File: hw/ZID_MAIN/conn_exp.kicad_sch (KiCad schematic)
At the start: 31 parts, among them J10 USB-C PWR ONLY, J8 BRK EXP SOCKET, J9 Z80-TARGET, U24 74AHCT125

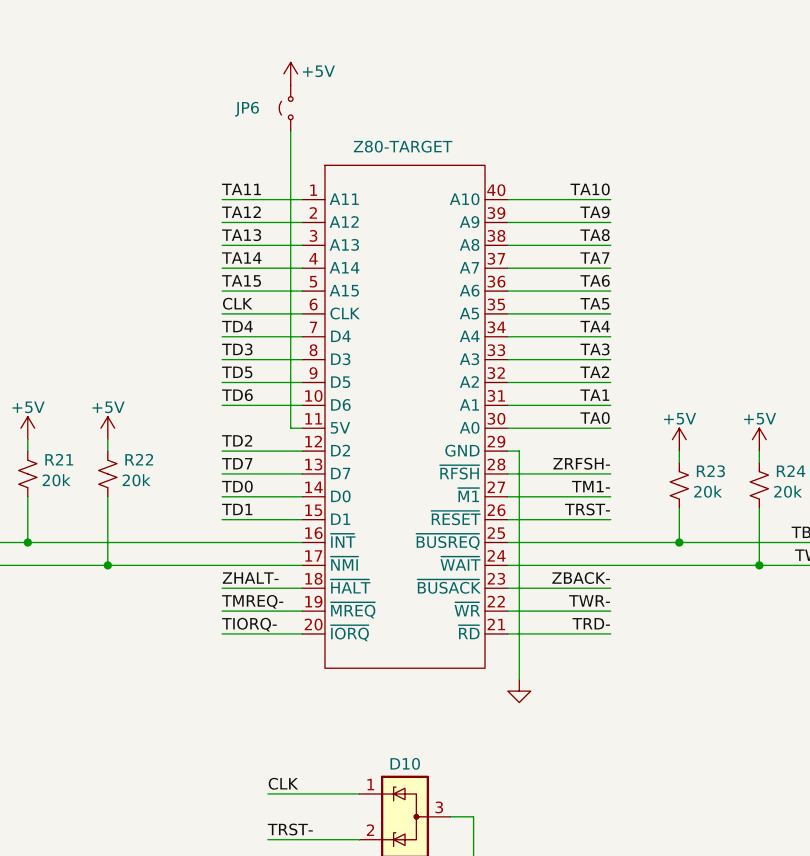
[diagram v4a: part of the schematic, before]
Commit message: Footprints assigned
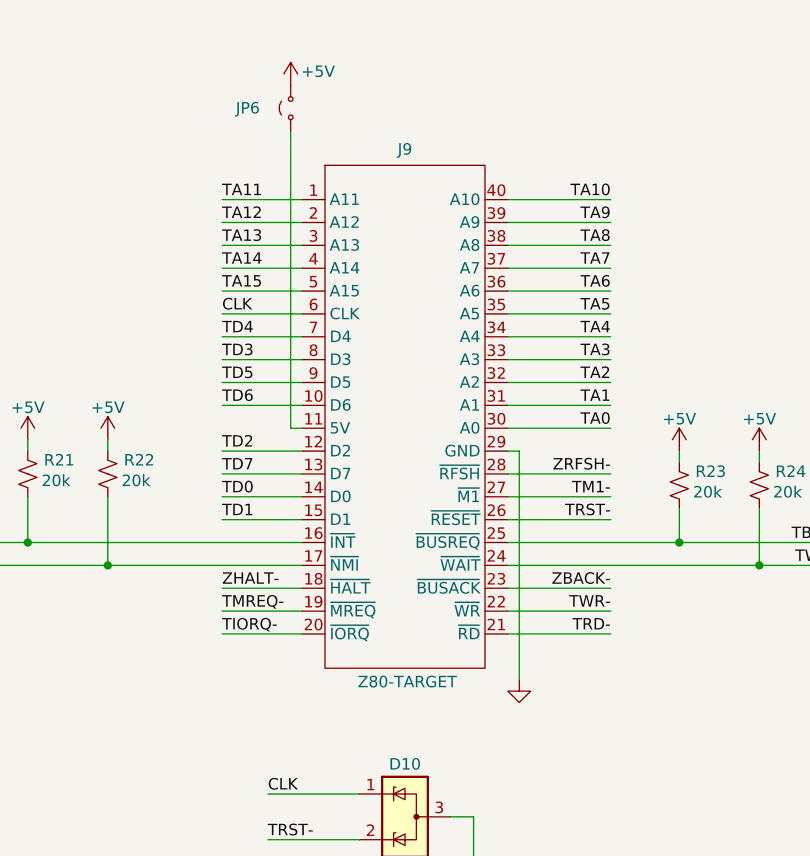
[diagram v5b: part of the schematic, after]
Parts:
- D1: value LED RED -> LED BLUE
- D10, D11: footprint Package_TO_SOT_SMD:SOT-23-3 -> Package_TO_SOT_SMD:SOT-323_SC-70
- D12: footprint Diode_SMD:D_SOD-523 -> AES_Library:DO-214AB-AES
- D2: value LED RED -> LED YELLOW
- D4: value LED RED -> LED ORANGE
- H1, H2, H3, H4: footprint (none) -> MountingHole:MountingHole_3.2mm_M3
- J8: footprint (none) -> Connector_PinSocket_2.54mm:PinSocket_1x28_P2.54mm_Vertical
- J9: footprint Connector_PinHeader_2.00mm:PinHeader_2x20_P2.00mm_Vertical -> AES_Library:CviLux_CF25401D0-05-NH_FFC-FPC-AES
- JP5, JP6, JP7: footprint (none) -> Connector_PinHeader_2.00mm:PinHeader_1x02_P2.00mm_Vertical
- R19, R20, R21, R22, R23, R24, R25, R26: footprint (none) -> Resistor_SMD:R_0805_2012Metric
- U24: footprint (none) -> Package_SO:SOIC-14_3.9x8.7mm_P1.27mm
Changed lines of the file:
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@@
 			)
 		)
-		(property "Footprint" ""
+		(property "Footprint" "MountingHole:MountingHole_3.2mm_M3"
 			(at 391.16 275.59 0)
 			(effects
@@
 			)
 		)
-		(property "Footprint" "Diode_SMD:D_SOD-523"
+		(property "Footprint" "AES_Library:DO-214AB-AES"
 			(at 256.54 268.605 0)
 			(effects
@@
 			)
 		)
-		(property "Footprint" ""
+		(property "Footprint" "Resistor_SMD:R_0805_2012Metric"
 			(at 187.96 62.23 0)
 			(effects
@@
 			)
 		)
-		(property "Value" "LED RED"
+		(property "Value" "LED ORANGE"
 			(at 217.424 76.454 0)
 			(effects
@@
 			)
 		)
-		(property "Footprint" ""
+		(property "Footprint" "MountingHole:MountingHole_3.2mm_M3"
 			(at 398.78 275.59 0)
 			(effects
@@
 			)
 		)
-		(property "Footprint" ""
+		(property "Footprint" "Connector_PinHeader_2.00mm:PinHeader_1x02_P2.00mm_Vertical"
 			(at 107.95 27.94 0)
 			(effects
@@
 			)
 		)
-		(property "Footprint" ""
+		(property "Footprint" "Connector_PinHeader_2.00mm:PinHeader_1x02_P2.00mm_Vertical"
 			(at 290.83 274.32 0)
 			(effects
@@
 			)
 		)
-		(property "Footprint" ""
+		(property "Footprint" "MountingHole:MountingHole_3.2mm_M3"
 			(at 383.54 275.59 0)
 			(effects
@@
 			)
 		)
-		(property "Footprint" "Package_TO_SOT_SMD:SOT-23-3"
+		(property "Footprint" "Package_TO_SOT_SMD:SOT-323_SC-70"
 			(at 130.81 91.44 0)
 			(effects
@@
 			)
 		)
-		(property "Footprint" ""
+		(property "Footprint" "Package_SO:SOIC-14_3.9x8.7mm_P1.27mm"
 			(at 199.39 64.77 0)
 			(effects
@@
 			)
 		)
-		(property "Footprint" ""
+		(property "Footprint" "Resistor_SMD:R_0805_2012Metric"
 			(at 187.96 48.26 0)
 			(effects
@@
 			)
 		)
-		(property "Footprint" ""
+		(property "Footprint" "Resistor_SMD:R_0805_2012Metric"
 			(at 78.74 68.58 0)
 			(effects
@@
 			)
 		)
-		(property "Footprint" ""
+		(property "Footprint" "Connector_PinSocket_2.54mm:PinSocket_1x28_P2.54mm_Vertical"
 			(at 114.3 193.04 0)
 			(effects
@@
 			)
 		)
-		(property "Footprint" ""
+		(property "Footprint" "Resistor_SMD:R_0805_2012Metric"
 			(at 53.34 210.82 0)
 			(effects
@@
 		(dnp no)
 		(property "Reference" "J9"
-			(at 120.65 60.96 0)
+			(at 120.65 32.512 0)
 			(effects
 				(font
 					(size 1.27 1.27)
 				)
-				(hide yes)
 			)
 		)
 		(property "Value" "Z80-TARGET"
-			(at 120.396 32.258 0)
+			(at 120.904 91.694 0)
 			(effects
 				(font
@@
 			)
 		)
-		(property "Footprint" "Connector_PinHeader_2.00mm:PinHeader_2x20_P2.00mm_Vertical"
+		(property "Footprint" "AES_Library:CviLux_CF25401D0-05-NH_FFC-FPC-AES"
 			(at 120.65 60.96 0)
 			(effects
@@
 			)
 		)
-		(property "Footprint" "Package_TO_SOT_SMD:SOT-23-3"
+		(property "Footprint" "Package_TO_SOT_SMD:SOT-323_SC-70"
 			(at 130.81 106.68 0)
 			(effects
@@
 			)
 		)
-		(property "Value" "LED RED"
+		(property "Value" "LED BLUE"
 			(at 217.424 34.544 0)
 			(effects
@@
 			)
 		)
-		(property "Footprint" ""
+		(property "Footprint" "MountingHole:MountingHole_3.2mm_M3"
 			(at 375.92 275.59 0)
 			(effects
@@
 			)
 		)
-		(property "Footprint" ""
+		(property "Footprint" "Package_SO:SOIC-14_3.9x8.7mm_P1.27mm"
 			(at 199.39 36.83 0)
 			(effects
@@
 			)
 		)
-		(property "Footprint" ""
+		(property "Footprint" "Package_SO:SOIC-14_3.9x8.7mm_P1.27mm"
 			(at 29.21 290.83 0)
 			(effects
@@
 			)
 		)
-		(property "Footprint" ""
+		(property "Footprint" "Connector_PinHeader_2.00mm:PinHeader_1x02_P2.00mm_Vertical"
 			(at 74.93 87.63 0)
 			(effects
@@
 			)
 		)
-		(property "Value" "LED RED"
+		(property "Value" "LED YELLOW"
 			(at 217.424 48.514 0)
 			(effects
@@
 			)
 		)
-		(property "Footprint" ""
+		(property "Footprint" "Package_SO:SOIC-14_3.9x8.7mm_P1.27mm"
 			(at 199.39 78.74 0)
 			(effects
@@
 			)
 		)
-		(property "Footprint" ""
+		(property "Footprint" "Package_SO:SOIC-14_3.9x8.7mm_P1.27mm"
 			(at 199.39 50.8 0)
 			(effects
@@
 			)
 		)
-		(property "Footprint" ""
+		(property "Footprint" "Resistor_SMD:R_0805_2012Metric"
 			(at 87.63 68.58 0)
 			(effects
@@
 			)
 		)
-		(property "Footprint" ""
+		(property "Footprint" "Resistor_SMD:R_0805_2012Metric"
 			(at 151.13 69.85 0)
 			(effects
@@
 			)
 		)
-		(property "Footprint" ""
+		(property "Footprint" "Resistor_SMD:R_0805_2012Metric"
 			(at 60.96 210.82 0)
 			(effects
@@
 			)
 		)
-		(property "Footprint" ""
+		(property "Footprint" "Resistor_SMD:R_0805_2012Metric"
 			(at 160.02 69.85 0)
 			(effects

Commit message: Bypass caps
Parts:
- added C10, C11, C12, C13, C14, C15, C16, C17, C18, C19, C20, C21, C22, C23, C24, C25, C26, C27, C28, C29, C3, C30, C31, C32, C33, C4, C5, C6, C7, C8, C9: 0.1uF, Capacitor_SMD:C_0603_1608Metric, symbol Device:C_Small
- added C34: 220uF, Capacitor_THT:CP_Radial_D6.3mm_P2.50mm, symbol Device:C_Polarized_Small_US
- added SPARE1: ~, AES_Library:SPARE-and-SOIC-16-AES, symbol AES_Library:SPARE-16-AES
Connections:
- net +5V: now also C10.2, C11.2, C12.2, C13.2, C14.2, C15.2, C17.2, C19.2, C21.2, C23.2, C24.2, C25.2, C26.2, C27.2, C28.2, C29.2, C3.2, C30.2, C31.2, C32.2, C33.2, C34.1, C4.2, C5.2, C6.2, C7.2, C8.2, C9.2
- net GND: now also C10.1, C11.1, C12.1, C13.1, C14.1, C15.1, C16.1, C17.1, C18.1, C19.1, C20.1, C21.1, C22.1, C23.1, C24.1, C25.1, C26.1, C27.1, C28.1, C29.1, C3.1, C30.1, C31.1, C32.1, C33.1, C34.2, C4.1, C5.1, C6.1, C7.1, C8.1, C9.1
- new net +3.3V: C16.2, C18.2, C20.2, C22.2

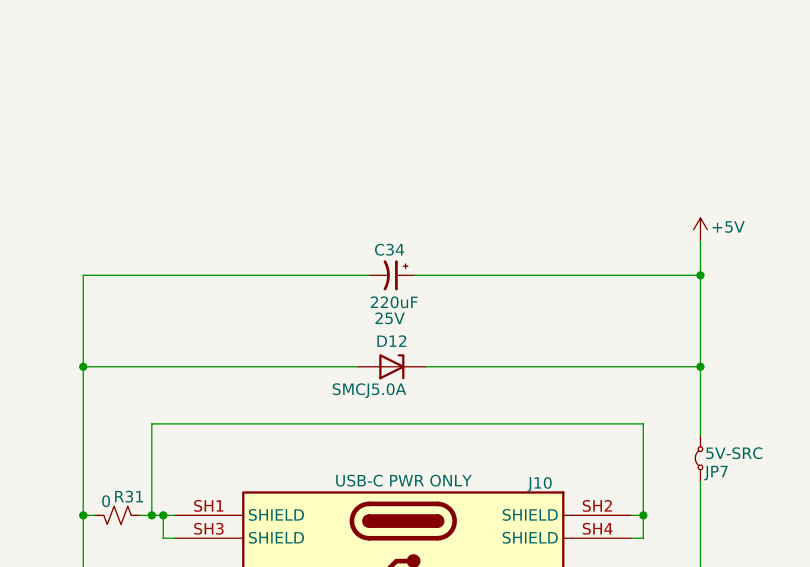
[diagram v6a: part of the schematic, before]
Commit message: 74LVC3G04, free up BUSACK_H and BUSACK_L.
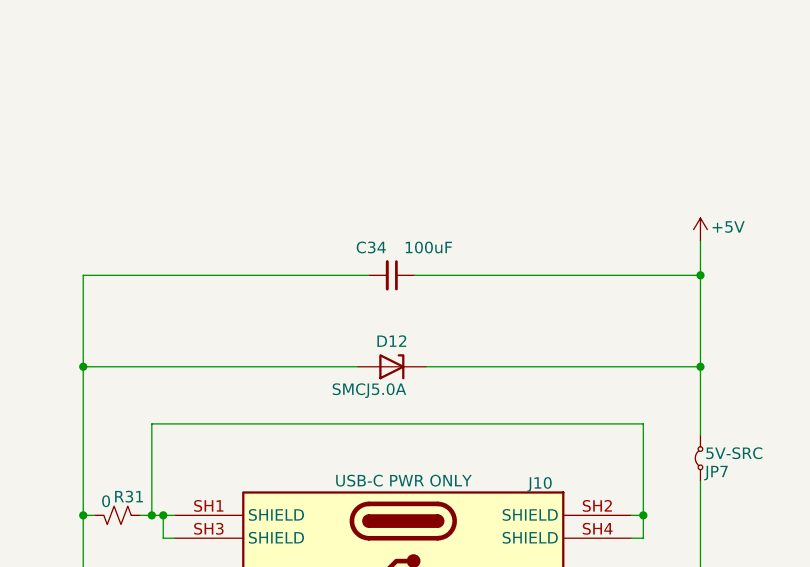
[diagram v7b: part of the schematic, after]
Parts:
- removed C34: 220uF, Capacitor_THT:CP_Radial_D6.3mm_P2.50mm, symbol Device:C_Polarized_Small_US
- added C34: 100uF, Capacitor_SMD:C_1210_3225Metric_Pad1.33x2.70mm_HandSolder, symbol Device:C_Small
- D12: footprint AES_Library:DO-214AB-AES -> Diode_SMD:D_SOD-523
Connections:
- net +5V: now also C34.1
- net GND: now also C34.2
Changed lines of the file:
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@@
 			)
 		)
-		(property "Footprint" "AES_Library:DO-214AB-AES"
+		(property "Footprint" "Diode_SMD:D_SOD-523"
 			(at 256.54 268.605 0)
 			(effects
@@
 	)
 	(symbol
-		(lib_id "Device:C_Polarized_Small_US")
+		(lib_id "power:GND")
+		(at 198.12 71.12 0)
+		(unit 1)
+		(exclude_from_sim no)
+		(in_bom yes)
+		(on_board yes)
+		(dnp no)
+		(property "Reference" "#PWR091"
+			(at 198.12 77.47 0)
+			(effects
+				(font
+					(size 1.27 1.27)
+				)
+				(hide yes)
+			)
+		)
+		(property "Value" "GND"
+			(at 201.422 73.406 0)
+			(effects
+				(font
+					(size 1.27 1.27)
+				)
+				(hide yes)
+			)
+		)
+		(property "Footprint" ""
+			(at 198.12 71.12 0)
+			(effects
+				(font
+					(size 1.27 1.27)
+				)
+				(hide yes)
+			)
+		)
+		(property "Datasheet" ""
+			(at 198.12 71.12 0)
+			(effects
+				(font
+					(size 1.27 1.27)
+				)
+				(hide yes)
+			)
+		)
+		(property "Description" "Power symbol creates a global label with name \"GND\" , ground"
+			(at 198.12 71.12 0)
+			(effects
+				(font
+					(size 1.27 1.27)
+				)
+				(hide yes)
+			)
+		)
+		(pin "1"
+		)
+		(instances
+			(project "ZID_MAIN"
+				(path "/2be47242-6db6-4d8d-b590-8c682dee013e/85d5adae-afa2-47ff-bde7-22bb8340c4cf"
+					(reference "#PWR091")
+					(unit 1)
+				)
+			)
+		)
+	)
+	(symbol
+		(lib_id "Device:C_Small")
 		(at 256.54 254 270)
 		(unit 1)
@@
 		(dnp no)
 		(property "Reference" "C34"
-			(at 256.286 251.206 90)
-			(effects
-				(font
-					(size 1.27 1.27)
-				)
-			)
-		)
-		(property "Value" "220uF"
-			(at 256.794 257.048 90)
-			(effects
-				(font
-					(size 1.27 1.27)
-				)
-			)
-		)
-		(property "Footprint" "Capacitor_THT:CP_Radial_D6.3mm_P2.50mm"
+			(at 254.254 250.952 90)
+			(effects
+				(font
+					(size 1.27 1.27)
+				)
+			)
+		)
+		(property "Value" "100uF"
+			(at 260.604 250.952 90)
+			(effects
+				(font
+					(size 1.27 1.27)
+				)
+			)
+		)
+		(property "Footprint" "Capacitor_SMD:C_1210_3225Metric_Pad1.33x2.70mm_HandSolder"
 			(at 256.54 254 0)
 			(effects
@@
 			)
 		)
-		(property "Description" "Polarized capacitor, small US symbol"
+		(property "Description" "Unpolarized capacitor, small symbol"
 			(at 256.54 254 0)
 			(effects
@@
 			)
 		)
-		(property "Voltage" "25V"
-			(at 256.286 258.826 90)
-			(effects
-				(font
-					(size 1.27 1.27)
-				)
-			)
-		)
 		(property "CPU" ""
-			(at 256.54 254 90)
+			(at 256.54 254 0)
 			(effects
 				(font
@@
 		)
 		(property "OPT-A" ""
-			(at 256.54 254 90)
+			(at 256.54 254 0)
 			(effects
 				(font
@@
 		)
 		(property "OPT-B" ""
-			(at 256.54 254 90)
-			(effects
-				(font
-					(size 1.27 1.27)
-				)
-				(hide yes)
-			)
+			(at 256.54 254 0)
+			(effects
+				(font
+					(size 1.27 1.27)
+				)
+				(hide yes)
+			)
+		)
+		(pin "1"
 		)
 		(pin "2"
 		)
-		(pin "1"
-		)
 		(instances
 			(project "ZID_MAIN"
@@
 					(unit 1)
 				)
-			)
-		)
-	)
-	(symbol
-		(lib_id "power:GND")
-		(at 198.12 71.12 0)
-		(unit 1)
-		(exclude_from_sim no)
-		(in_bom yes)
-		(on_board yes)
-		(dnp no)
-		(property "Reference" "#PWR091"
-			(at 198.12 77.47 0)
-			(effects
-				(font
-					(size 1.27 1.27)
-				)
-				(hide yes)
-			)
-		)
-		(property "Value" "GND"
-			(at 201.422 73.406 0)
-			(effects
-				(font
-					(size 1.27 1.27)
-				)
-				(hide yes)
-			)
-		)
-		(property "Footprint" ""
-			(at 198.12 71.12 0)
-			(effects
-				(font
-					(size 1.27 1.27)
-				)
-				(hide yes)
-			)
-		)
-		(property "Datasheet" ""
-			(at 198.12 71.12 0)
-			(effects
-				(font
-					(size 1.27 1.27)
-				)
-				(hide yes)
-			)
-		)
-		(property "Description" "Power symbol creates a global label with name \"GND\" , ground"
-			(at 198.12 71.12 0)
-			(effects
-				(font
-					(size 1.27 1.27)
-				)
-				(hide yes)
-			)
-		)
-		(pin "1"
-		)
-		(instances
-			(project "ZID_MAIN"
-				(path "/2be47242-6db6-4d8d-b590-8c682dee013e/85d5adae-afa2-47ff-bde7-22bb8340c4cf"
-					(reference "#PWR091")
-					(unit 1)
-				)
